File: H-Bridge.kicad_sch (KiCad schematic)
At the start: 19 parts, among them J2 Conn_01x02_Pin, Q1 IRF640NPBF, Q2 IRF640NPBF, Q3 IRF640NPBF, Q4 IRF640NPBF, U3 IR2110, U4 IR2110

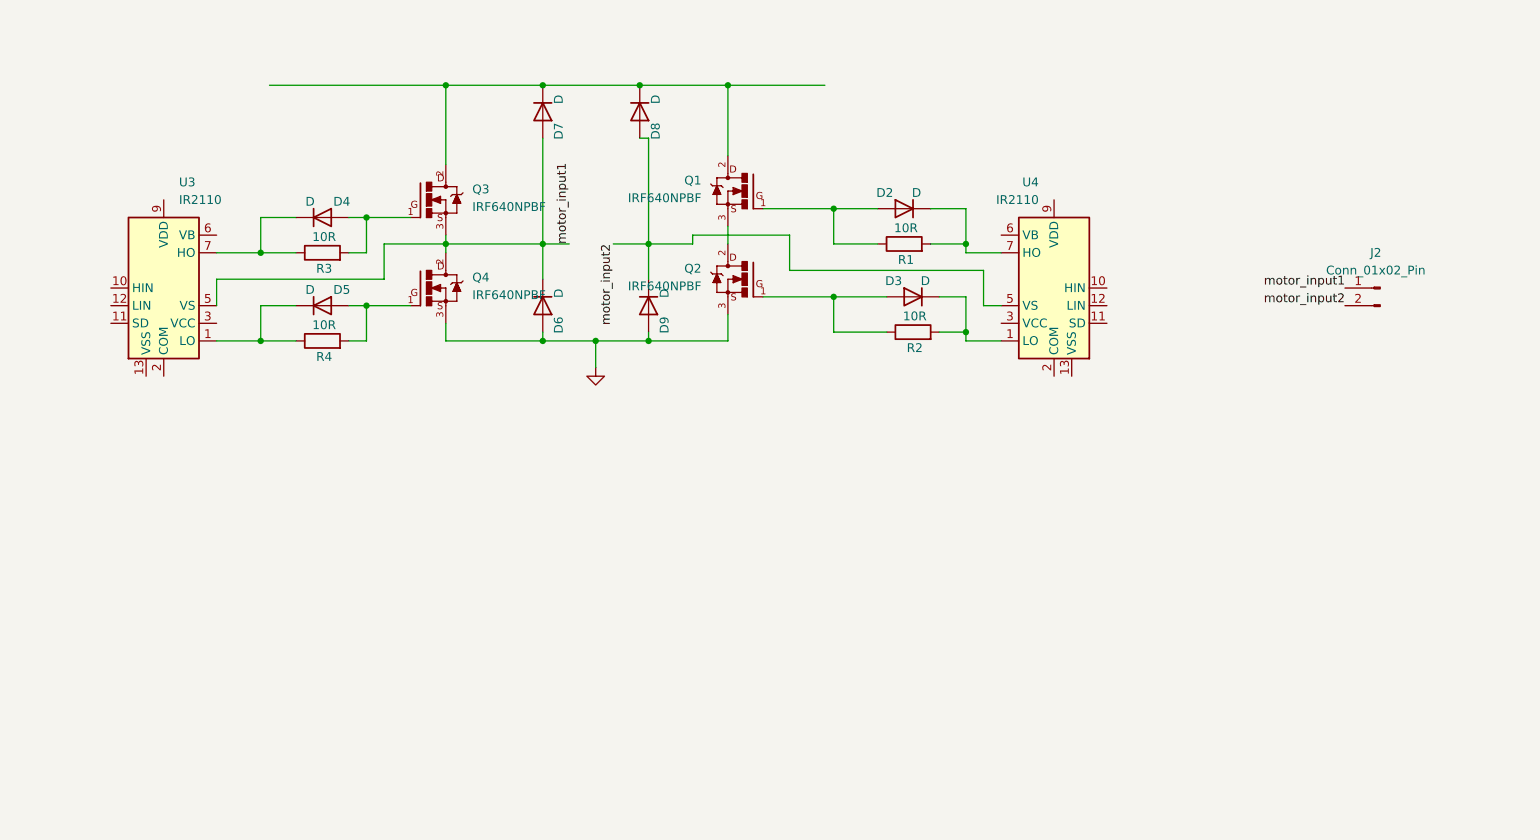
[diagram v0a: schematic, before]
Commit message: Done upto shunt circuit, H-bridge, remaining Loogic
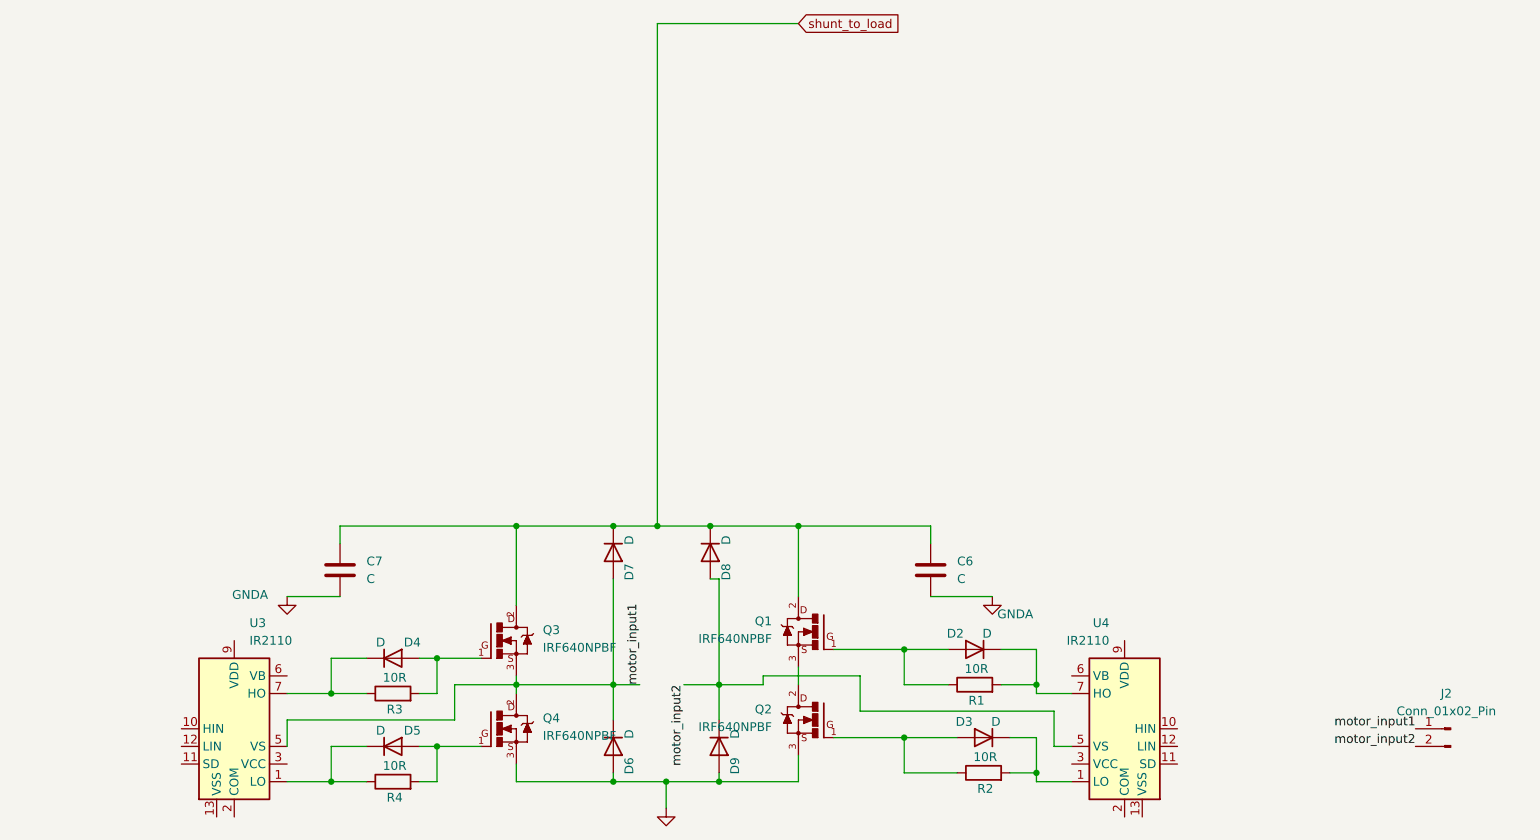
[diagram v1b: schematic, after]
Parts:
- added C6, C7: C, symbol Device:C
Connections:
- net shunt_to_load: now reaches D7.1 (K), D8.1 (K), Q1.2, Q3.2
- net shunt_to_load: now also C6.1, C7.1
- new net GNDA: C6.2, C7.2
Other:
- moved on the sheet: D2, D3, D4, D5, D6, D7, D8, D9, J2, Q1, Q2, Q3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

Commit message: Finished all parts of schematic: power, H-bridge, logic and shunt schematics
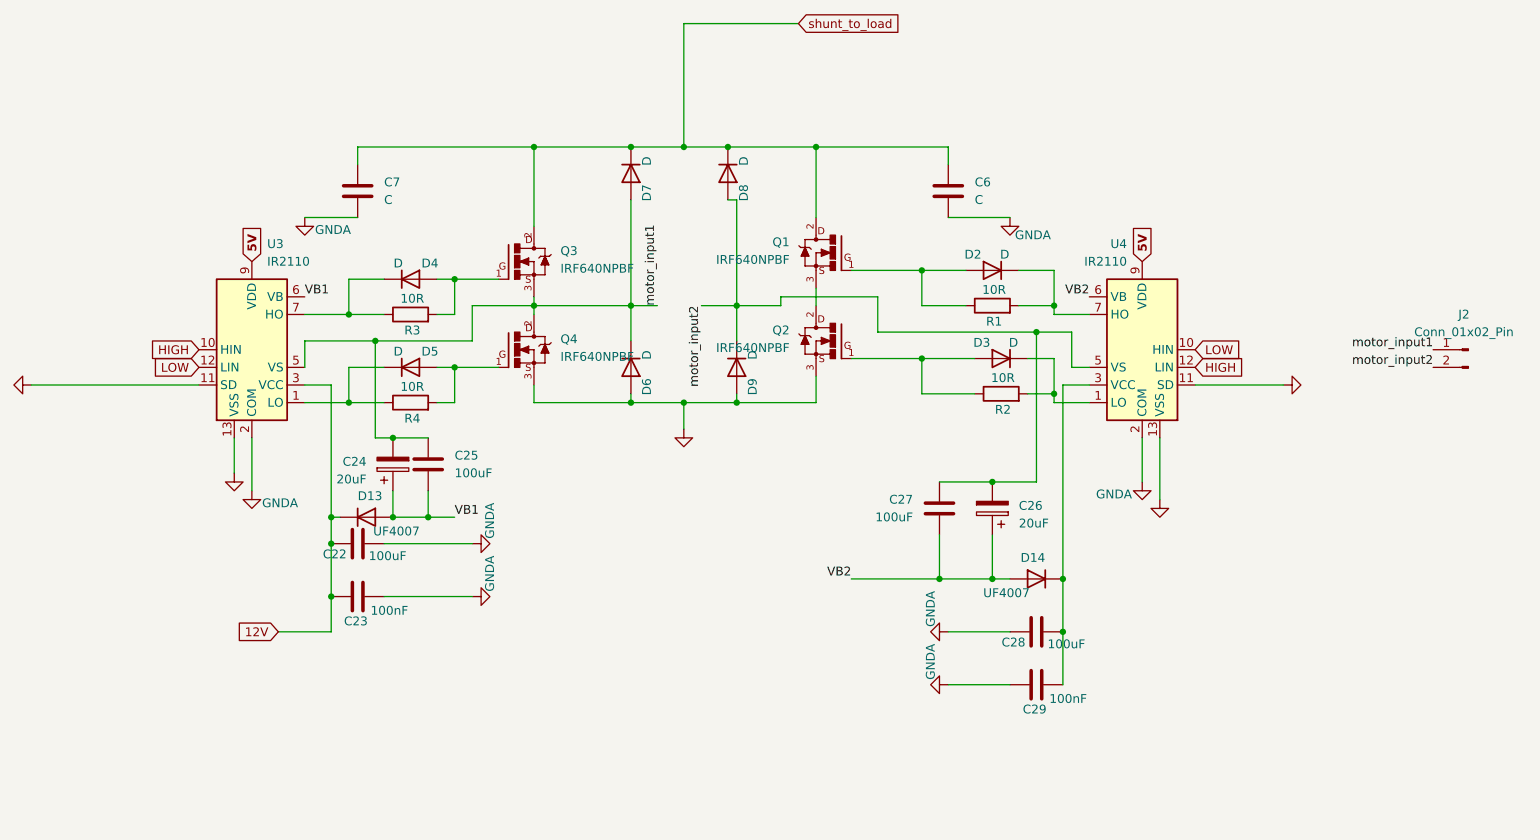
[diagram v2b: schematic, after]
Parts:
- added C22, C25, C27, C28: 100uF, symbol Device:C
- added C23, C29: 100nF, symbol Device:C
- added C24, C26: 20uF, symbol Device:C_Polarized
- added D13, D14: UF4007, symbol Device:D
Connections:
- net GND: now also U3.11 (SD), U3.13 (VSS), U4.11 (SD), U4.13 (VSS)
- net GNDA: now also U3.2 (COM), U4.2 (COM), C22.2, C23.2, C28.1, C29.1
- net motor_input1: now also C24.2, C25.1
- net motor_input2: now also C26.2, C27.1
- net HIGH: now reaches U3.10 (HIN)
- net HIGH: now also U4.12 (LIN)
- net LOW: now reaches U3.12 (LIN)
- net LOW: now also U4.10 (HIN)
- net 12V: now reaches U3.3 (VCC)
- net 12V: now also C22.1, C23.1, D13.1 (K)
- net VB1: now reaches U3.6 (VB)
- net VB1: now also C24.1, C25.2, D13.2 (A)
- net 5V: now reaches U3.9 (VDD)
- net 5V: now also U4.9 (VDD)
- net at U4.3 (VCC): now also C28.2, C29.2, D14.1 (K)
- net VB2: now reaches U4.6 (VB)
- net VB2: now also C26.1, C27.2, D14.2 (A)
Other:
- moved on the sheet: C6, C7, D2, D3, D4, D5, D6, D7, D8, D9, J2, Q1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
